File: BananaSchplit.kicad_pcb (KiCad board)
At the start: 2 copper layers, 77 x 32 mm, 53 parts, among them J1 Screw_Terminal_01x02, J2 Screw_Terminal_01x02, J3 Screw_Terminal_01x02, J4 Screw_Terminal_01x02, Q1 AO3401A, Q2 AO3401A, U1 TPS5430DDA, U2 TPS65131RGER

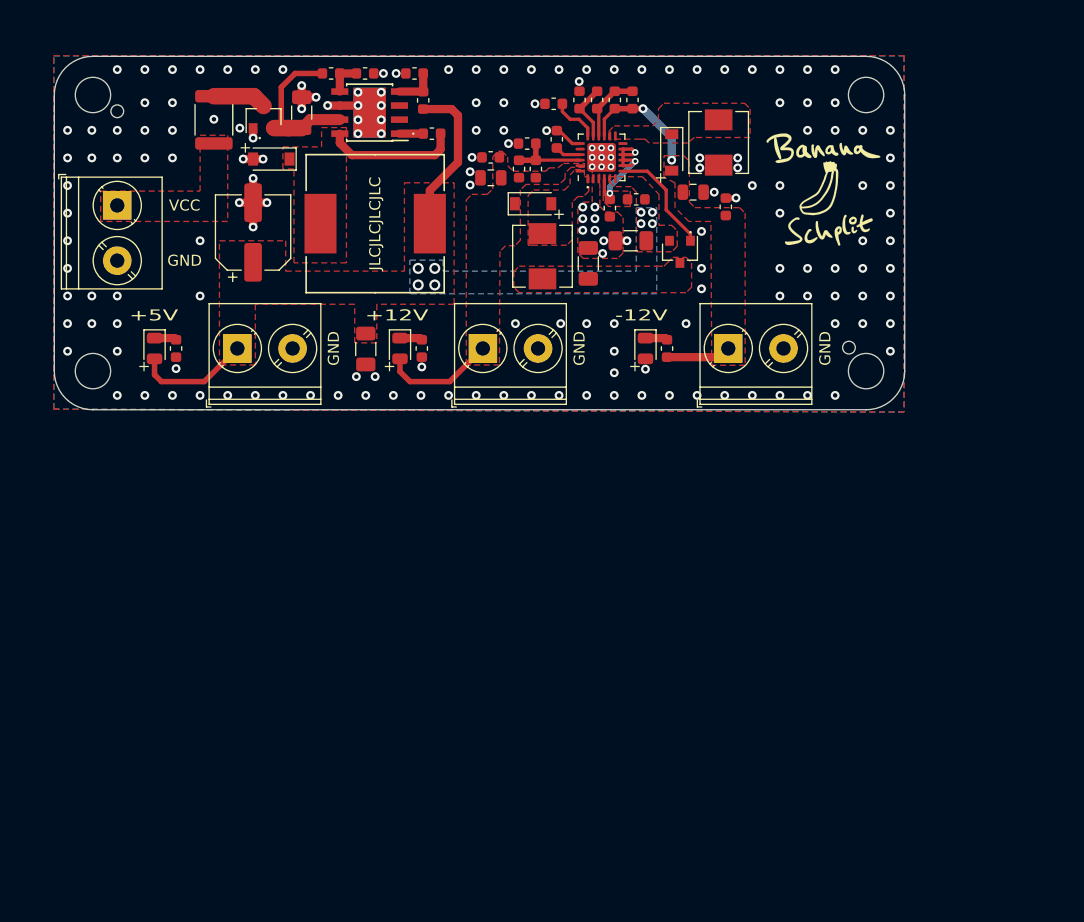
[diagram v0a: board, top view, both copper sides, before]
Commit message: filtering + euroheaders
added more filtering/capacitance.
changed layout, added eurroack power headers and more inputs
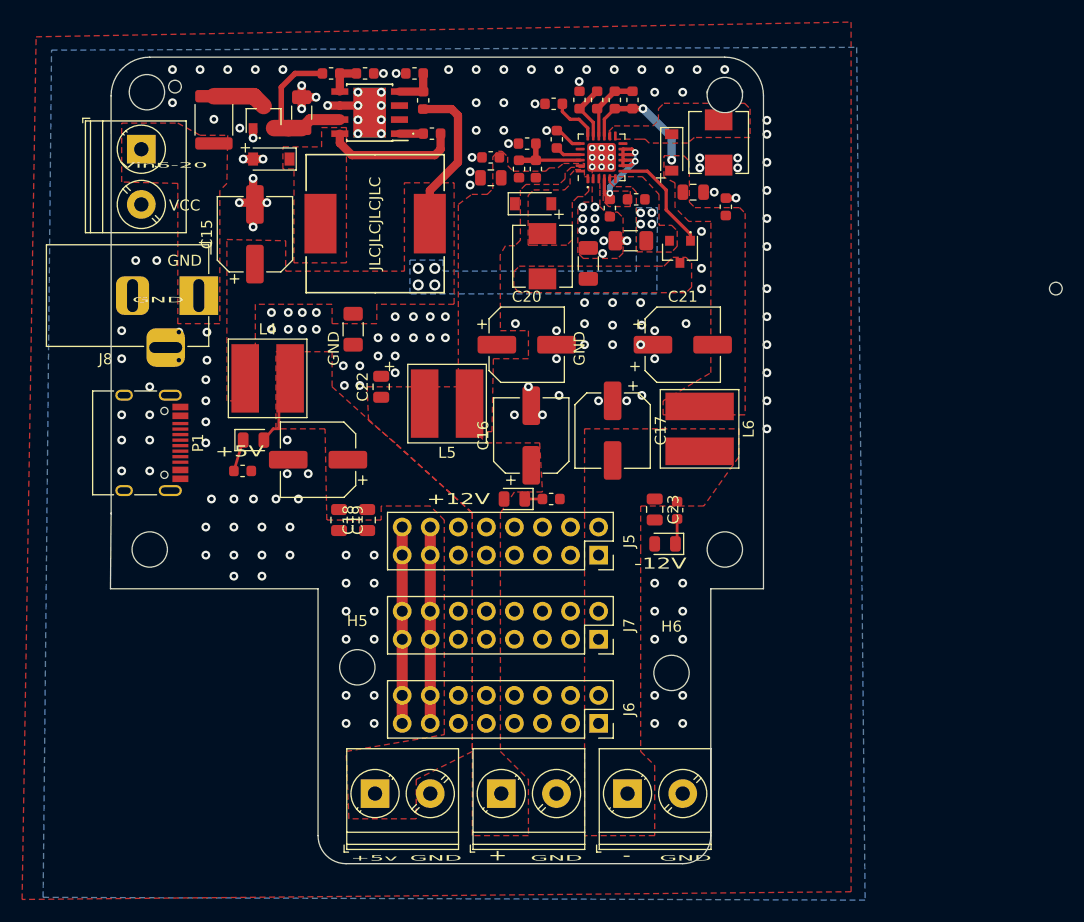
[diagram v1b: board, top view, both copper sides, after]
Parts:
- removed G***: LOGO, BananSchplitSilk:BananaSchplitSilkLogoDrawn
- added C15: 220u, Capacitor_SMD:CP_Elec_6.3x7.7, F.Cu at (37.5, 31.9)
- added C16: 220u, Capacitor_SMD:CP_Elec_6.3x7.7, F.Cu at (62.5, 50.1)
- added C17: 220u, Capacitor_SMD:CP_Elec_6.3x7.7, F.Cu at (69.8, 49.7)
- added C18: 22u, Capacitor_SMD:C_0805_2012Metric, F.Cu at (47.6, 57.8)
- added C19: 22u, Capacitor_SMD:C_0805_2012Metric, F.Cu at (45.1, 57.8)
- added C20: 220u, Capacitor_SMD:CP_Elec_6.3x7.7, F.Cu at (62.1, 41.9)
- added C21: 220u, Capacitor_SMD:CP_Elec_6.3x7.7, F.Cu at (76.2, 41.9)
- added C22: 22u, Capacitor_SMD:C_0805_2012Metric, F.Cu at (48.9, 45.7)
- added C23: 22u, Capacitor_SMD:C_0805_2012Metric, F.Cu at (73.7, 56.8)
- added H5: MountingHole, MountingHole:MountingHole_3.2mm_M3, F.Cu at (46.7, 71.1)
- added H6: MountingHole, MountingHole:MountingHole_3.2mm_M3, F.Cu at (75.2, 71.6)
- added J5: Conn_02x08_Odd_Even, Connector_PinSocket_2.54mm:PinSocket_2x08_P2.54mm_Vertical, F.Cu at (68.6, 61.0)
- added J6: Conn_02x08_Odd_Even, Connector_PinSocket_2.54mm:PinSocket_2x08_P2.54mm_Vertical, F.Cu at (68.6, 76.2)
- added J7: Conn_02x08_Odd_Even, Connector_PinSocket_2.54mm:PinSocket_2x08_P2.54mm_Vertical, F.Cu at (68.6, 68.6)
- added J8: Barrel_Jack, Connector_BarrelJack:BarrelJack_Horizontal, F.Cu at (32.4, 37.5)
- added L4: 1 uH, BananSchplitSilk:TYS60281R0N-10, F.Cu at (38.6, 45.0)
- added L5: 1 uH, BananSchplitSilk:TYS60281R0N-10, F.Cu at (54.9, 47.2)
- added L6: 1 uH, BananSchplitSilk:TYS60281R0N-10, F.Cu at (77.7, 49.5)
- added P1: USB_C_Plug_USB2.0, Connector_USB:USB_C_Receptacle_HRO_TYPE-C-31-M-12, F.Cu at (26.7, 50.8)
- F1: value 1A -> 500mA
- Q1, Q2: value AO3401A -> AO3407A
- moved J2 42.2 mm to (48.3, 82.5)
- moved J4 41.3 mm to (71.2, 82.5)
- moved J3 40.3 mm to (59.8, 82.5)
- moved C4 21.4 mm to (43.2, 52.3), turned to 180 degrees
- moved H2 20.6 mm to (80.0, 60.5)
- moved REF** 19.5 mm to (110.0, 36.8)
- moved R13 18.0 mm to (64.3, 55.9), turned to 180 degrees
- moved D6 17.8 mm to (74.6, 59.9), turned to 180 degrees
- moved D5 17.1 mm to (61.0, 55.9), turned to 180 degrees
- moved H1 17.0 mm to (27.9, 60.5)
- moved R14 14.7 mm to (75.7, 56.9), turned to 270 degrees
- moved H4 12.8 mm to (80.0, 19.3)
- moved R12 12.6 mm to (36.3, 53.3), turned to 180 degrees
- moved D4 12.2 mm to (37.3, 50.5), turned to 0 degrees
- moved REF** 5.68 mm to (30.2, 18.5)
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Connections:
- C10 pad 1: +12V -> Net-(C10-Pad1)
- C11 pad 2: -12V -> Net-(C11-Pad2)
- C14 pad 1: -12V -> Net-(C11-Pad2)
- C3 pad 1: +5V -> powertosplit
- C5 pad 1: +5V -> powertosplit
- C9 pad 1: +12V -> Net-(C10-Pad1)
- D2 pad 1: +12V -> Net-(C10-Pad1)
- D3 pad 2: -12V -> Net-(C11-Pad2)
- L1 pad 2: +5V -> powertosplit
- Q2 pad 2: +5V -> powertosplit
- R10 pad 2: +12V -> Net-(C10-Pad1)
- R11 pad 2: -12V -> Net-(C11-Pad2)
- R3 pad 2: +5V -> powertosplit
- R5 pad 2: +5V -> powertosplit
- R6 pad 2: +12V -> Net-(C10-Pad1)
- R9 pad 1: -12V -> Net-(C11-Pad2)
- U2 pad 15: -12V -> Net-(C11-Pad2)
- U2 pad 23: +12V -> Net-(C10-Pad1)
- U2 pad 5: +5V -> powertosplit
- U2 pad 6: +5V -> powertosplit
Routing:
- net +5V: track 24.7 -> 6.39 mm, vias 8 -> 0
- net gate: track 0.00 -> 17.8 mm
- net cv: track 0.00 -> 17.8 mm
- net -12V: track 17.0 -> 0.00 mm, vias 2 -> 0
- net powertosplit: track 0.00 -> 14.2 mm, vias 0 -> 8
- net Net-(C11-Pad2): track 0.00 -> 11.2 mm, vias 0 -> 2
- net +12V: track 10.3 -> 0.00 mm
- net Net-(D4-Pad1): track 2.01 -> 2.92 mm
- net Net-(C7-Pad1): track 12.3 -> 13.1 mm
- net VCC: vias 0 -> 1
- net Net-(J8-Pad2): vias 0 -> 1
- net GND: vias 178 -> 184
- net (no net): vias 0 -> 14
- added copper zone on F.Cu, net Net-(C10-Pad1)
- added copper zone on F.Cu, net Net-(C11-Pad2)
- added copper zone on B.Cu, net powertosplit
- added copper zone on F.Cu, net powertosplit
- removed copper zone on B.Cu, net +5V
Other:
- board size 77 x 32 mm -> 59.1 x 73 mm
- board text added: "+5v"
- board text added: "-"
- board text added: "Vin6-20"
